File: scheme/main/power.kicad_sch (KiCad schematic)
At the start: 33 parts, among them U15 SCWN06B-15, U16 K7809-1000R3, U17 K7803-1000R3, U18 LD1117S50TR_SOT223, U19 IFX1117MEV33HTMA1, U20 K7805-1000R3

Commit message: replace some 220n capacitors with 100n
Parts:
- added C111, C112: 100nF, Capacitor_SMD:C_0805_2012Metric, symbol Device:C
- C61, C63: value 22uF -> 10uF
- C62, C64, C66, C68, C70, C72, C76, C78, C80, C82: value 220nF -> 100nF
- C65, C67, C81: value 47uF -> 22uF
- C69, C71: value 47uF -> 10uF
- C79: value 4.7uF -> 10uF
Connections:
- net +9V: now also C111.1, C112.1
- net GNDA: now also C111.2, C112.2
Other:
- moved on the sheet: NT1

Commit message: added L fuse & more
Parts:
- NT1, NT3, NT4: footprint (none) -> NetTie:NetTie-2_SMD_Pad0.5mm
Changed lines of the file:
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@@
 			)
 		)
-		(property "Footprint" ""
+		(property "Footprint" "NetTie:NetTie-2_SMD_Pad0.5mm"
 			(at 152.4 97.79 0)
 			(effects
@@
 			)
 		)
-		(property "Footprint" ""
+		(property "Footprint" "NetTie:NetTie-2_SMD_Pad0.5mm"
 			(at 31.75 64.77 0)
 			(effects
@@
 			)
 		)
-		(property "Footprint" ""
+		(property "Footprint" "NetTie:NetTie-2_SMD_Pad0.5mm"
 			(at 41.91 64.77 0)
 			(effects

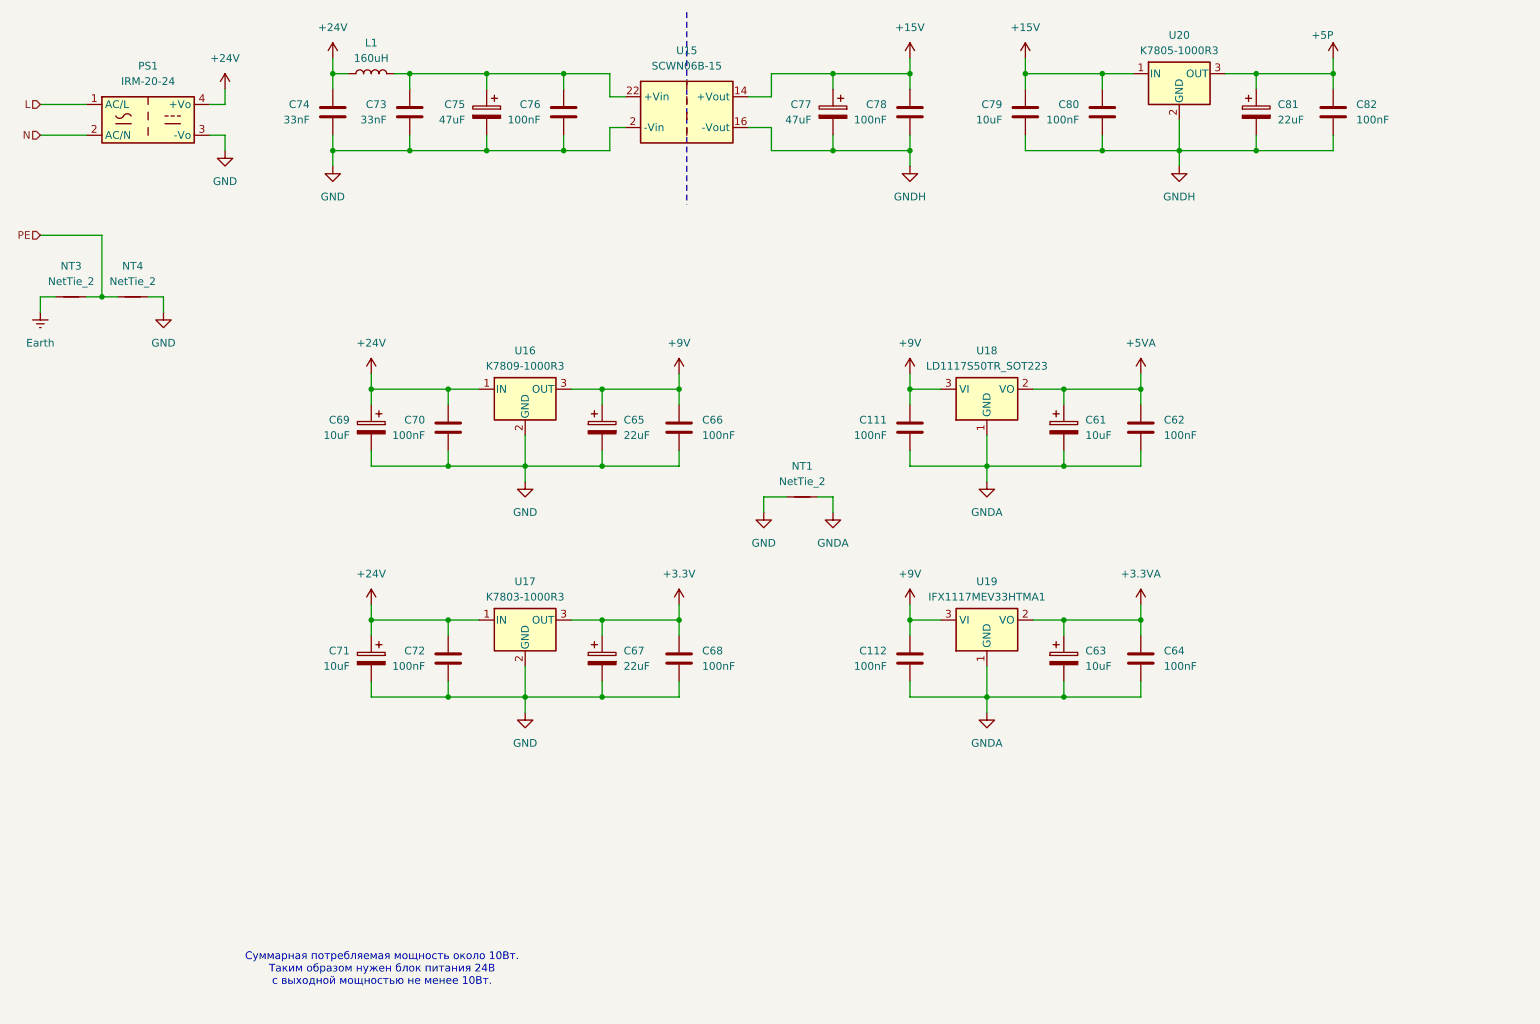
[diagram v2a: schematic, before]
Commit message: added 24V & GND to DO terminal & more
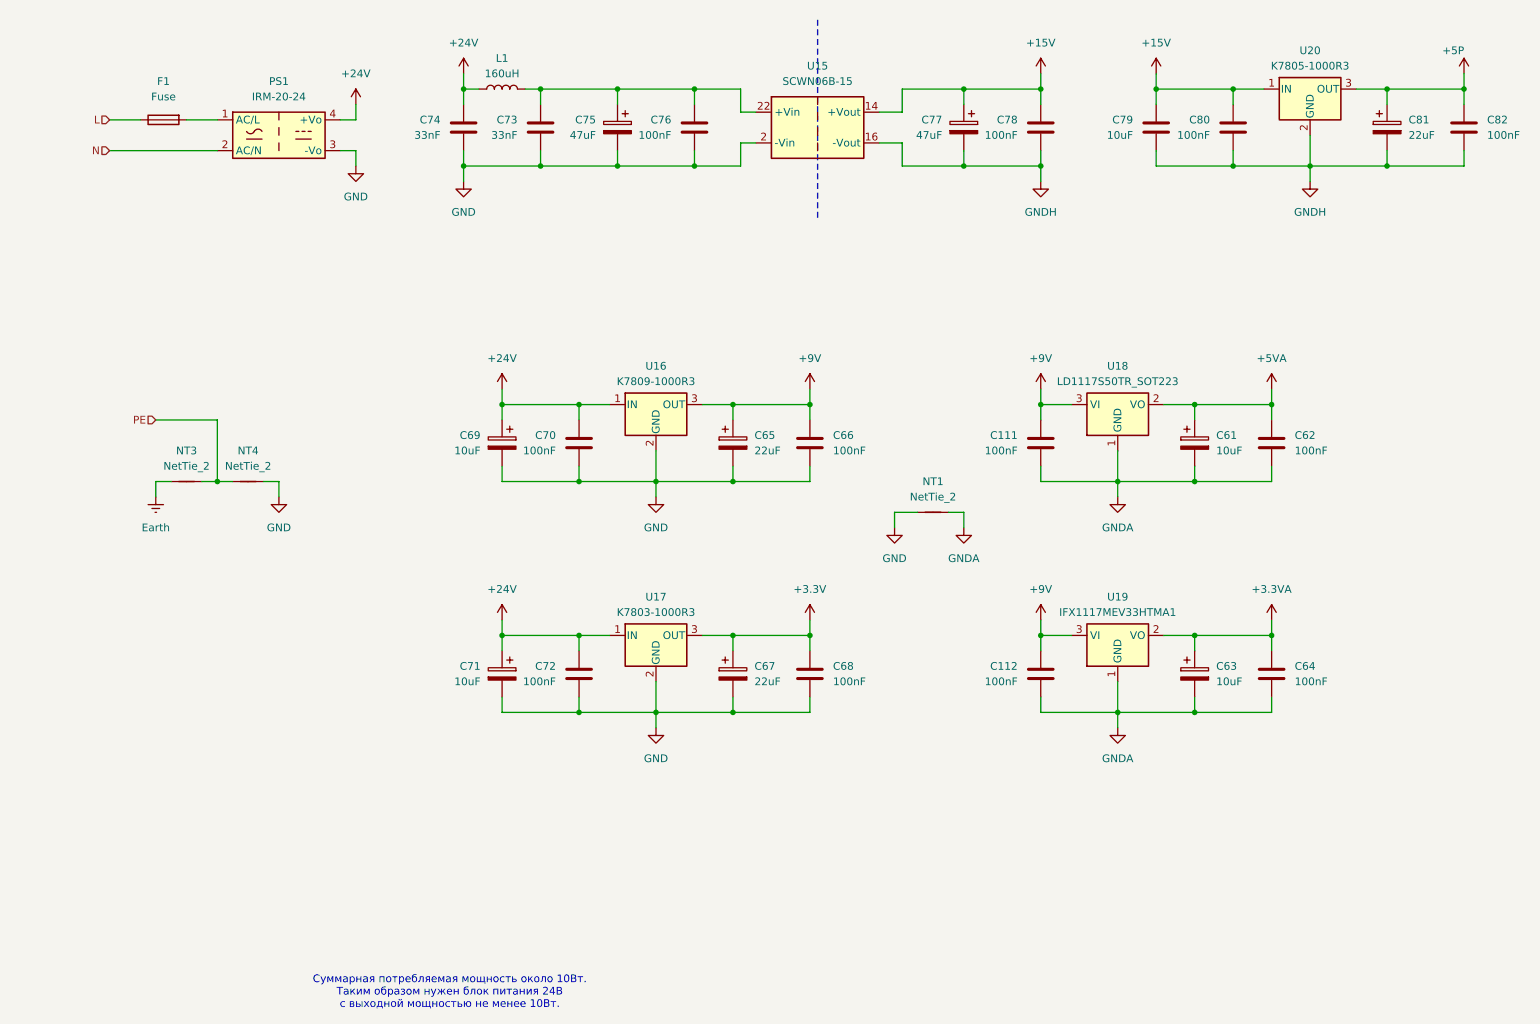
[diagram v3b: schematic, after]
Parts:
- added F1: Fuse, symbol Device:Fuse
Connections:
- net L: now also F1.1; no longer PS1.1 (AC/L)
- new net: F1.2, PS1.1 (AC/L)
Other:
- moved on the sheet: C111, C112, C61, C62, C63, C64, C65, C66, C67, C68, C69, C70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

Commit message: sheets titles
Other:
- title: (none) -> Питание
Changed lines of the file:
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@@
 	(generator_version "8.0")
 	(paper "A4")
+	(title_block
+		(title "Питание")
+	)
 	(junction
 		(at 204.47 95.25)

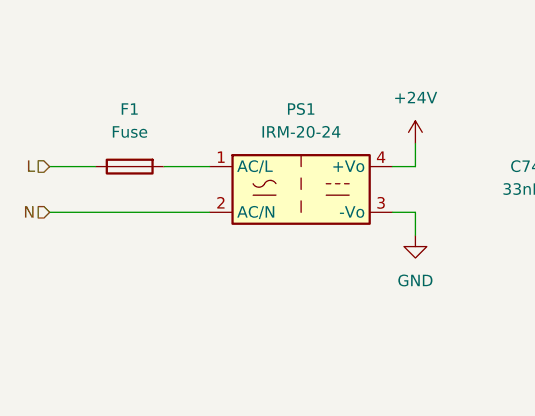
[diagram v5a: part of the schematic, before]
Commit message: added fuses & inductanses
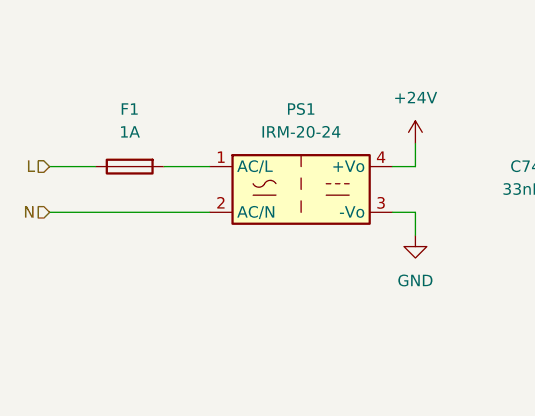
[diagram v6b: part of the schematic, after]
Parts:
- F1: value Fuse -> 1A
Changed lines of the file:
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@@
 			)
 		)
-		(property "Value" "Fuse"
+		(property "Value" "1A"
 			(at 46.99 31.75 90)
 			(effects

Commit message: fixed check errors
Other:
- moved on the sheet: NT1

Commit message: footprints set/changed
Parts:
- F1: footprint (none) -> main:Fuseholder_Clip-5x20mm_KLS5-266
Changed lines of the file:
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@@
 			)
 		)
-		(property "Footprint" ""
+		(property "Footprint" "main:Fuseholder_Clip-5x20mm_KLS5-266"
 			(at 46.99 33.782 90)
 			(effects
